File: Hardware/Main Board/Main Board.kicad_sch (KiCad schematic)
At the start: 22 parts, among them J1 Micro_SD_Card_Det1, SW1 SW_SPST, U1 ESP32-S3-WROOM-2

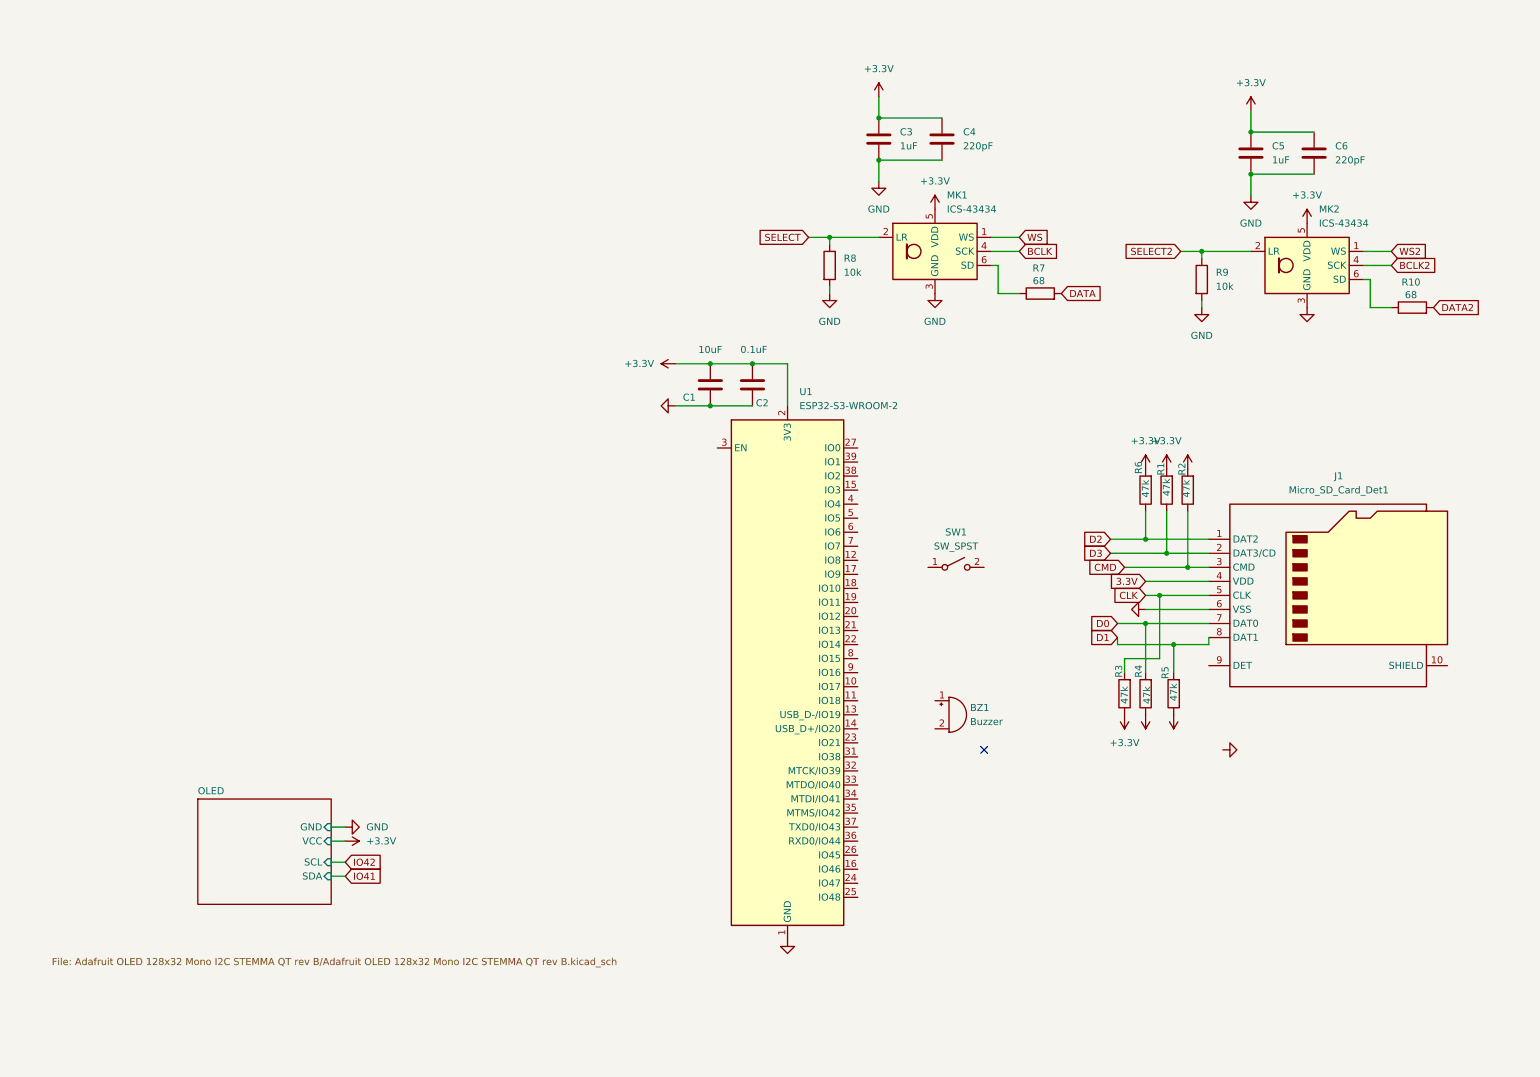
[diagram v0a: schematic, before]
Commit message: separated the microphone onto its own schematic as we won't be designing it. Updated the contact mic board
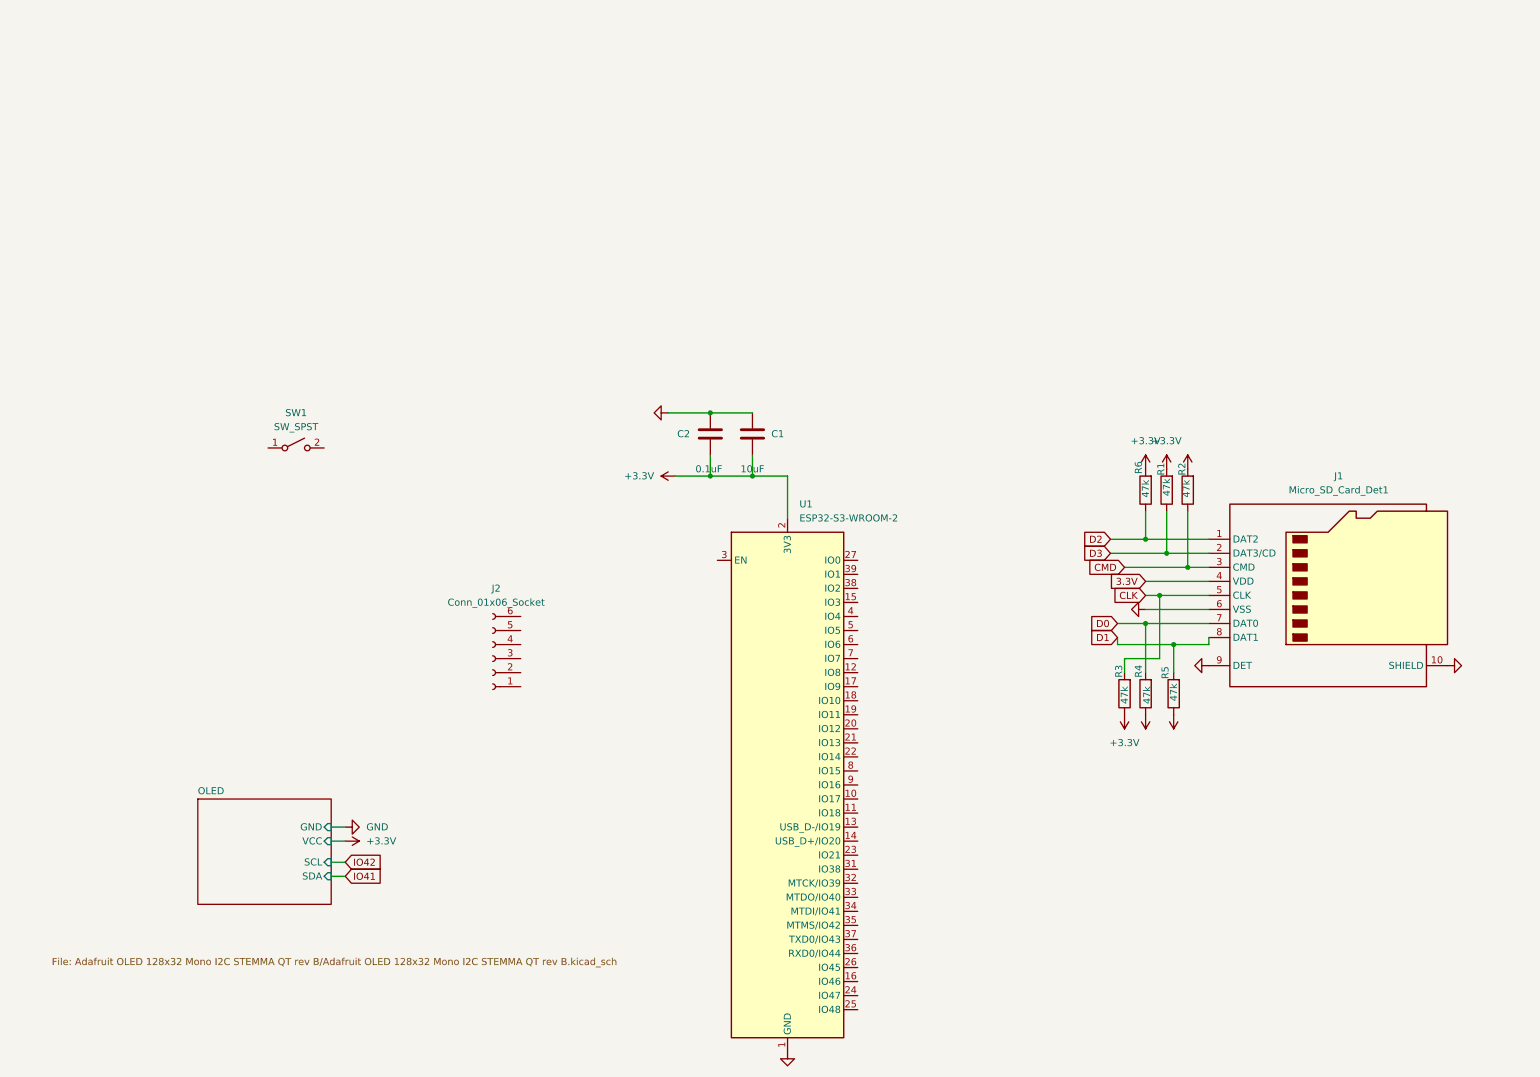
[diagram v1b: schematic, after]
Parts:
- removed BZ1: Buzzer, symbol Device:Buzzer
- removed C3, C5: 1uF, symbol Device:C
- removed C4, C6: 220pF, symbol Device:C
- removed MK1, MK2: ICS-43434, Sensor_Audio:InvenSense_ICS-43434-6_3.5x2.65mm, symbol Sensor_Audio:ICS-43434
- removed R10, R7: 68, symbol Device:R
- removed R8, R9: 10k, symbol Device:R
- added J2: Conn_01x06_Socket, symbol Connector:Conn_01x06_Socket
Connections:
- net GND: now also J1.10 (SHIELD), J1.9 (DET)
- no-connect marks 1 -> 0
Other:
- moved on the sheet: C1, C2, SW1, U1

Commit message: Added power management onto the main board schematic
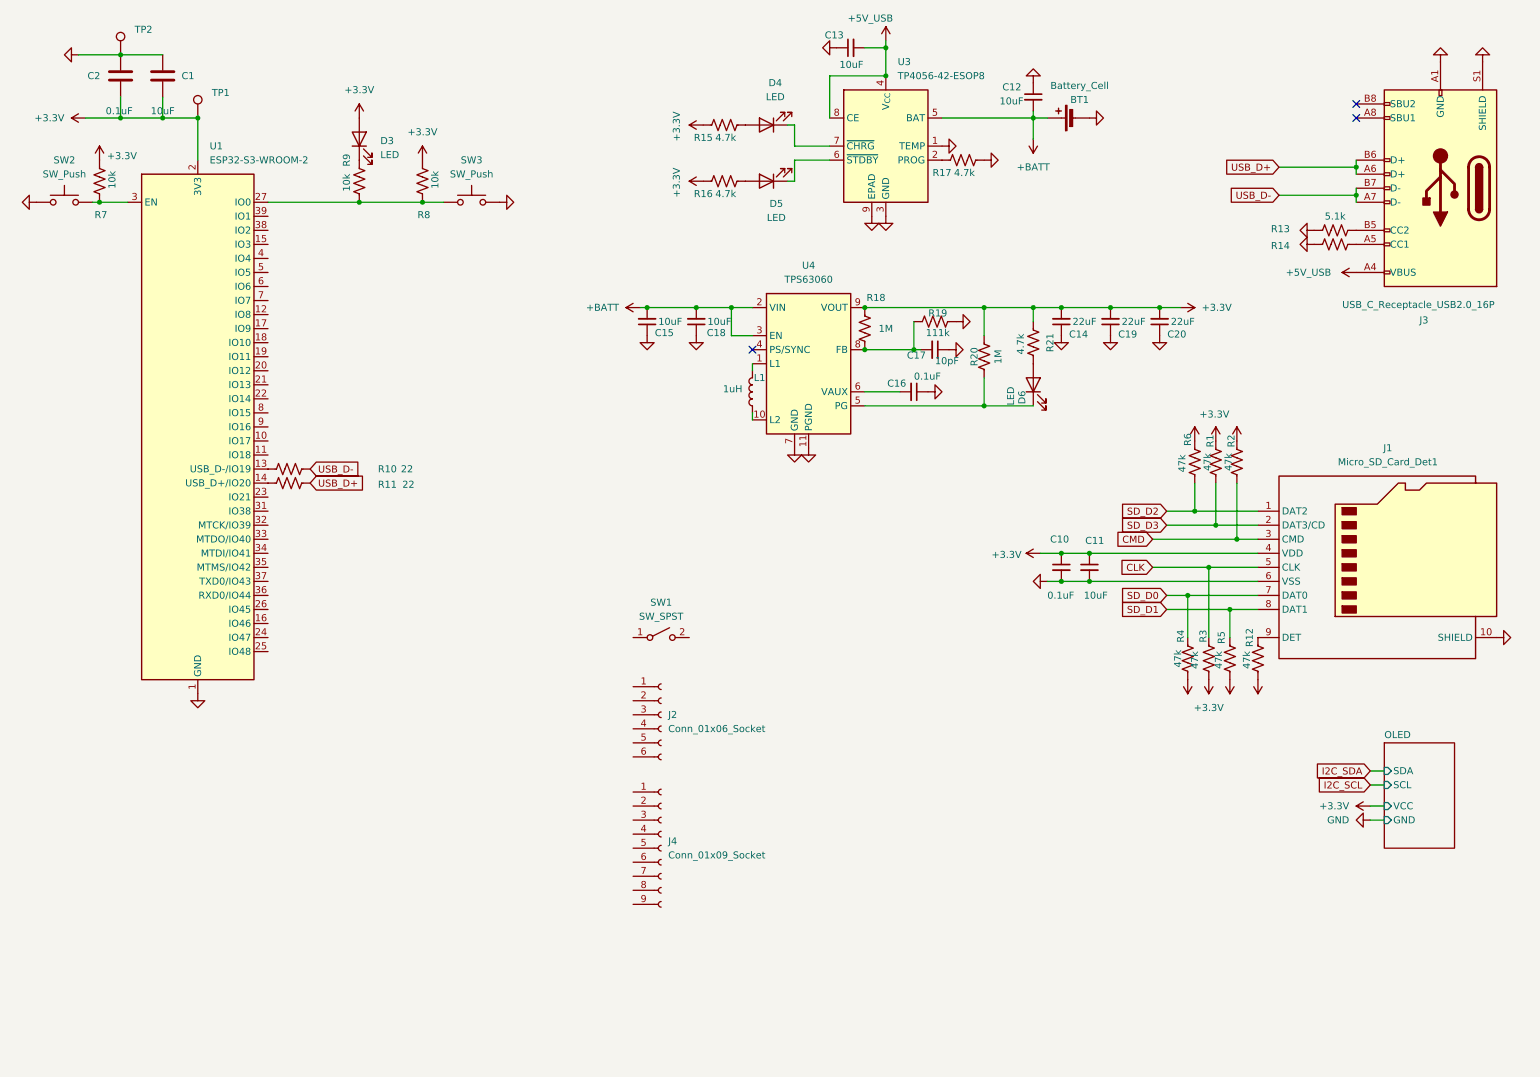
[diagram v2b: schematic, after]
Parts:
- added BT1: Battery_Cell, symbol Device:Battery_Cell
- added C10, C16: 0.1uF, symbol Device:C_Small
- added C11, C12, C13, C15, C18: 10uF, symbol Device:C_Small
- added C14, C19, C20: 22uF, symbol Device:C_Small
- added C17: 10pF, symbol Device:C_Small
- added D3, D4, D5, D6: LED, symbol Device:LED
- added J3: USB_C_Receptacle_USB2.0_16P, symbol Connector:USB_C_Receptacle_USB2.0_16P
- added J4: Conn_01x09_Socket, symbol Connector:Conn_01x09_Socket
- added L1: 1uH, symbol Device:L
- added R10, R11: 22, symbol Device:R_US
- added R12: 47k, symbol Device:R_US
- added R13, R14: 5.1k, symbol Device:R_US
- added R15, R16, R17, R21: 4.7k, symbol Device:R_US
- added R18, R20: 1M, symbol Device:R_US
- added R19: 111k, symbol Device:R_US
- added R7, R8, R9: 10k, symbol Device:R_US
- added SW2, SW3: SW_Push, symbol Switch:SW_Push
- added TP1, TP2: TestPoint, symbol Connector:TestPoint
- added U3: TP4056-42-ESOP8, Package_SO:SOIC-8-1EP_3.9x4.9mm_P1.27mm_EP2.41x3.3mm_ThermalVias, symbol Battery_Management:TP4056-42-ESOP8
- added U4: TPS63060, Package_SON:Texas_S-PWSON-N10_ThermalVias, symbol Regulator_Switching:TPS63060
- R1, R2, R3, R4, R5, R6: symbol Device:R -> Device:R_US
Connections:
- net 3.3V is gone; now on net +3.3V: J1.4 (VDD)
- net +3.3V: now also C10.1, C11.1, C14.2, C19.2, C20.2, D3.2 (A), R12.1, R15.2, R16.2, R18.2, R20.2, R21.2, R7.1, R8.1, TP1.1, U4.9 (VOUT)
- net GND: now also BT1.2 (-), C10.2, C11.2, C12.1, C13.1, C14.1, C15.1, C16.1, C17.1, C18.1, C19.1, C20.1, J3.A1 (GND), J3.A12 (GND), J3.B1 (GND), J3.B12 (GND), J3.S1 (SHIELD), R13.2, R14.2, R17.1, R19.1, SW2.1, SW3.2, TP2.1, U3.1 (TEMP), U3.3 (GND), U3.9 (EPAD), U4.11 (PGND), U4.7 (GND); no longer J1.9 (DET)
- net at U1.13 (USB_D-/IO19): now also R10.2
- net at U1.14 (USB_D+/IO20): now also R11.2
- net at U1.27 (IO0): now also R8.2, R9.1, SW3.1
- net at U1.3 (EN): now also R7.2, SW2.2
- net D0 renamed SD_D0
- net D1 renamed SD_D1
- net D2 renamed SD_D2
- net D3 renamed SD_D3
- new net: C17.2, R18.1, R19.2, U4.8 (FB)
- new net: D4.2 (A), R15.1
- new net: J3.A5 (CC1), R14.1
- new net: L1.1, U4.10 (L2)
- new net: L1.2, U4.1 (L1)
- new net: J3.B5 (CC2), R13.1
- new net: D5.1 (K), U3.6 (~{STDBY})
- new net: D5.2 (A), R16.1
- new net: D6.2 (A), R21.1
- new net: R17.2, U3.2 (PROG)
- new net: D4.1 (K), U3.7 (~{CHRG})
- new net: D6.1 (K), R20.1, U4.5 (PG)
- new net: D3.1 (K), R9.2
- new net: C16.2, U4.6 (VAUX)
- new net: J1.9 (DET), R12.2
- new net +5V_USB: C13.2, J3.A4 (VBUS), J3.A9 (VBUS), J3.B4 (VBUS), J3.B9 (VBUS), U3.4 (V_{CC}), U3.8 (CE)
- new net +BATT: BT1.1 (+), C12.2, C15.2, C18.2, U3.5 (BAT), U4.2 (VIN), U4.3 (EN)
- new net USB_D+: J3.A6 (D+), J3.B6 (D+), R11.1
- new net USB_D-: J3.A7 (D-), J3.B7 (D-), R10.1
- no-connect marks 0 -> 3
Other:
- moved on the sheet: C1, C2, J1, J2, SW1, U1
